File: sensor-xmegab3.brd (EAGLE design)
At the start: 55.6 x 39.3 mm, 46 parts, among them K1 SP6029TOP, M1 NRF24L01P-M, M2 DHT22-NP, Q1 IRLML2502, Q2 IRLML2502, U1 MCP1640C, X1 serial, X2 SPI/1W, X3 I2C, X4 ADC, X6 PDI

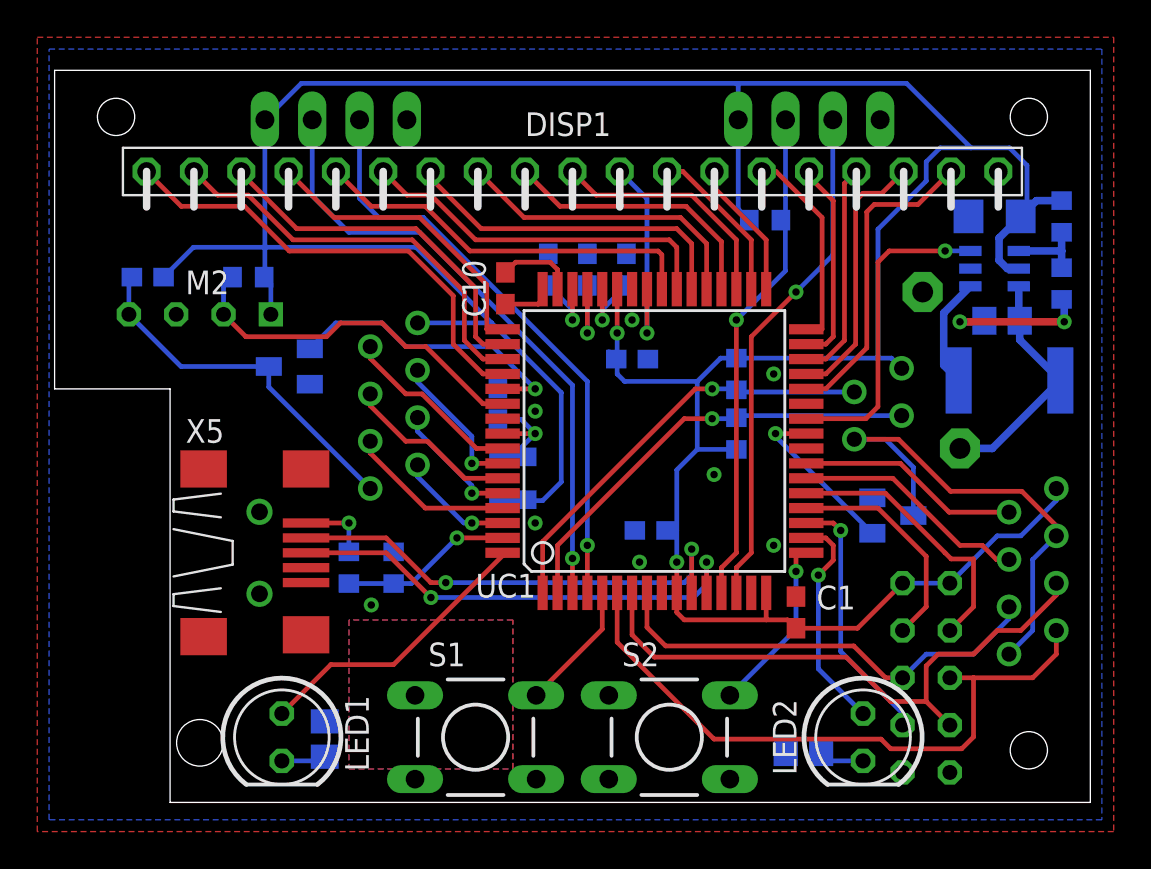
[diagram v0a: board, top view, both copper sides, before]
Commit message: pulldown for boostup enable line
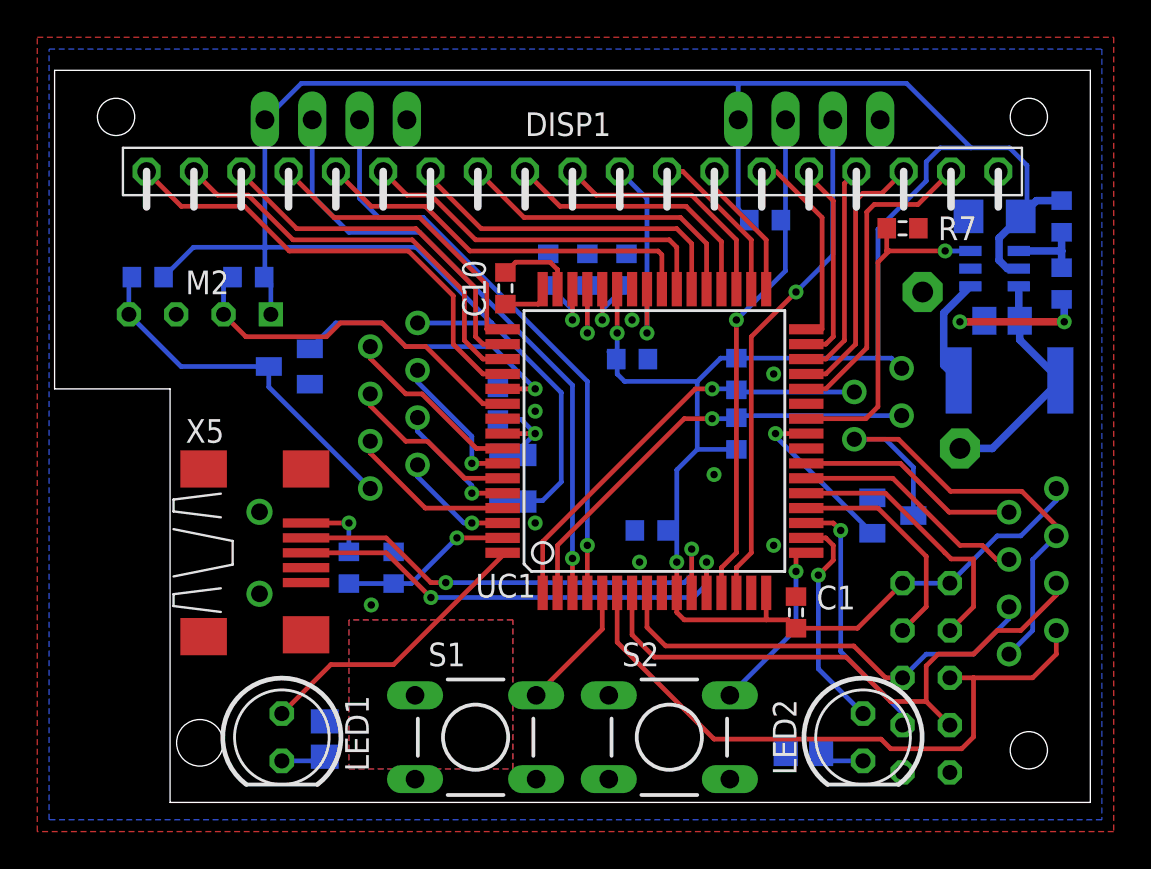
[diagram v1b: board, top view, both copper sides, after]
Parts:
- added R7: 10k, rcl:R0603
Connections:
- net GND: now also R7.2
- net PWRON: now also R7.1
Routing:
- net PWRON: track 17.1 -> 18.4 mm

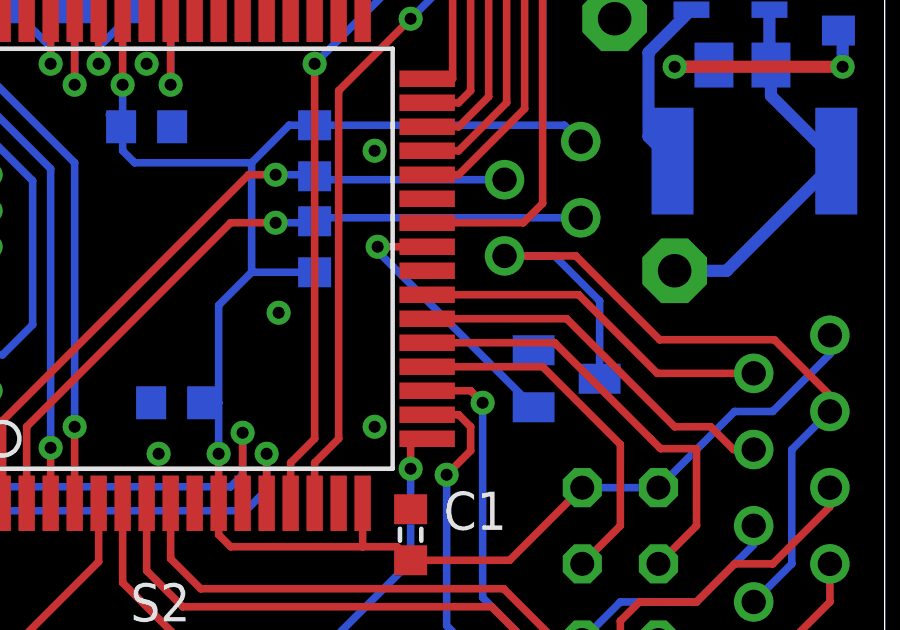
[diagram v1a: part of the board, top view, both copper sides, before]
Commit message: free seg14/15, can't be used with lcd in use
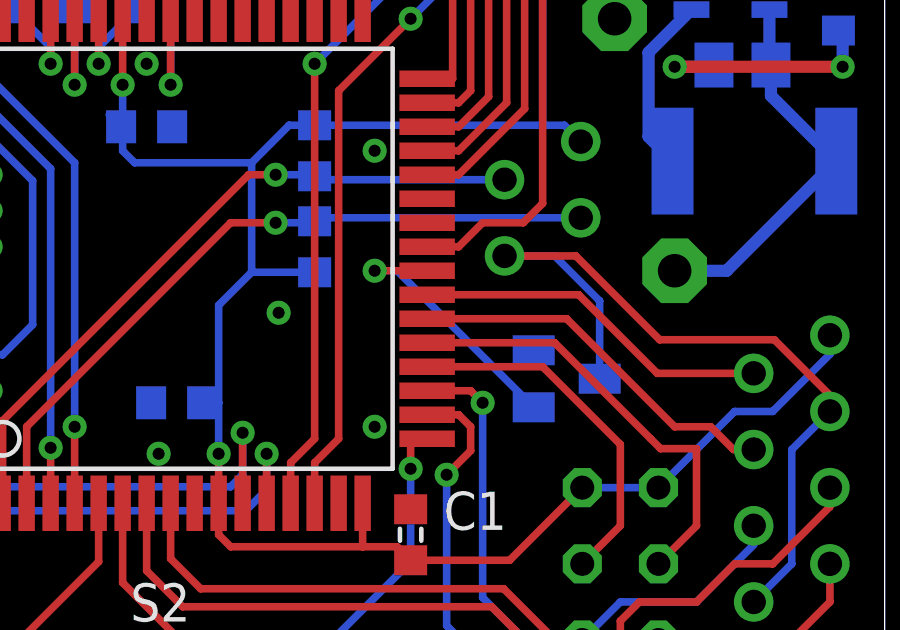
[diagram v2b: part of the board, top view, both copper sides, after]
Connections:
- new net SEG14: UC1.27
- new net SEG15: UC1.26
- net PWRON: now also UC1.25; no longer UC1.26
- net SPI1WON: now also UC1.24; no longer UC1.25
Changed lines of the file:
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@@
 <setting verticaltext="up"/>
 </settings>
-<grid distance="0.635" unitdist="mm" unit="mm" style="lines" multiple="1" display="yes" altdistance="5" altunitdist="mil" altunit="mic"/>
+<grid distance="0.4" unitdist="mm" unit="mm" style="lines" multiple="1" display="yes" altdistance="0.1" altunitdist="mm" altunit="mm"/>
 <layers>
 <layer number="1" name="Top" color="4" fill="1" visible="yes" active="yes"/>
@@
 <layer number="14" name="Route14" color="1" fill="6" visible="no" active="no"/>
 <layer number="15" name="Route15" color="4" fill="6" visible="no" active="no"/>
-<layer number="16" name="Bottom" color="1" fill="1" visible="no" active="yes"/>
+<layer number="16" name="Bottom" color="1" fill="1" visible="yes" active="yes"/>
 <layer number="17" name="Pads" color="2" fill="1" visible="yes" active="yes"/>
 <layer number="18" name="Vias" color="2" fill="1" visible="yes" active="yes"/>
@@
 <via x="48.005" y="31.805" extent="1-16" drill="0.4"/>
 <wire x1="45.005" y1="31.805" x2="48.005" y2="31.805" width="0.254" layer="1"/>
-<contactref element="UC1" pad="26"/>
-<wire x1="43.755" y1="22.8" x2="40.55" y2="22.8" width="0.254" layer="1"/>
 <contactref element="R7" pad="1"/>
 <wire x1="45.005" y1="31.805" x2="44.87" y2="31.805" width="0.254" layer="1"/>
 <wire x1="44.87" y1="31.805" x2="44.87" y2="33.02" width="0.254" layer="1"/>
+<contactref element="UC1" pad="25"/>
+<wire x1="43.755" y1="22.8" x2="42.4" y2="22.8" width="0.254" layer="1"/>
+<wire x1="42.4" y1="22.8" x2="41.6" y2="22" width="0.254" layer="1"/>
+<wire x1="41.6" y1="22" x2="40.55" y2="22" width="0.254" layer="1"/>
 </signal>
 <signal name="RFIRQ">
@@
 <contactref element="Q2" pad="1"/>
 <wire x1="44.1" y1="16.65" x2="43.75" y2="16.65" width="0.254" layer="16"/>
-<via x="38.9" y="22" extent="1-16" drill="0.4"/>
-<contactref element="UC1" pad="25"/>
-<wire x1="38.9" y1="22" x2="38.9" y2="21.85" width="0.254" layer="16"/>
-<wire x1="38.9" y1="21.85" x2="44.1" y2="16.65" width="0.254" layer="16"/>
-<wire x1="40.55" y1="22" x2="38.9" y2="22" width="0.254" layer="1"/>
+<contactref element="UC1" pad="24"/>
+<wire x1="44.1" y1="16.65" x2="39.55" y2="21.2" width="0.254" layer="16"/>
+<wire x1="39.55" y1="21.2" x2="38.8" y2="21.2" width="0.254" layer="16"/>
+<via x="38.8" y="21.2" extent="1-16" drill="0.4"/>
+<wire x1="38.8" y1="21.2" x2="40.55" y2="21.2" width="0.254" layer="1"/>
 </signal>
 <signal name="N$1">
@@
 </polygon>
 </signal>
+<signal name="SEG14">
+<contactref element="UC1" pad="27"/>
+</signal>
+<signal name="SEG15">
+<contactref element="UC1" pad="26"/>
+</signal>
 </signals>

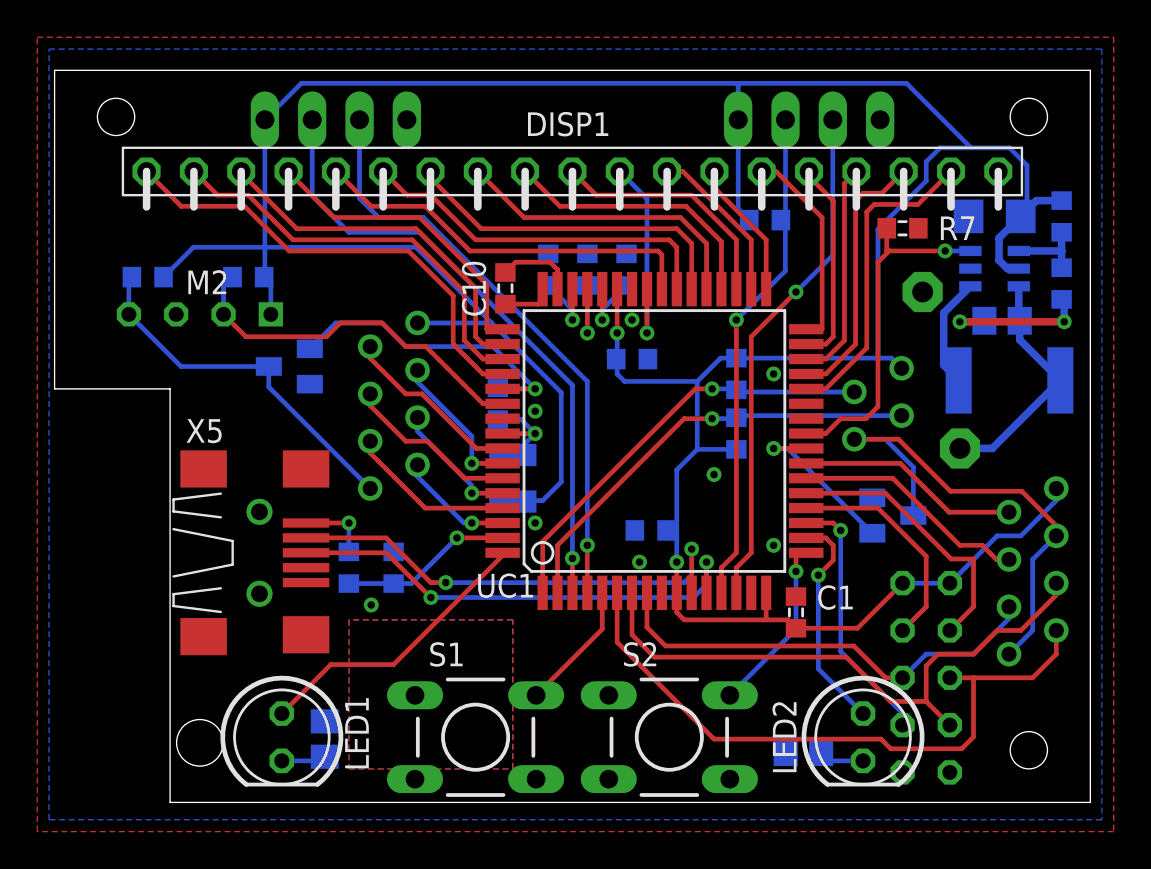
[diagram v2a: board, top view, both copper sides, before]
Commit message: reassign display pins
    fixes #1
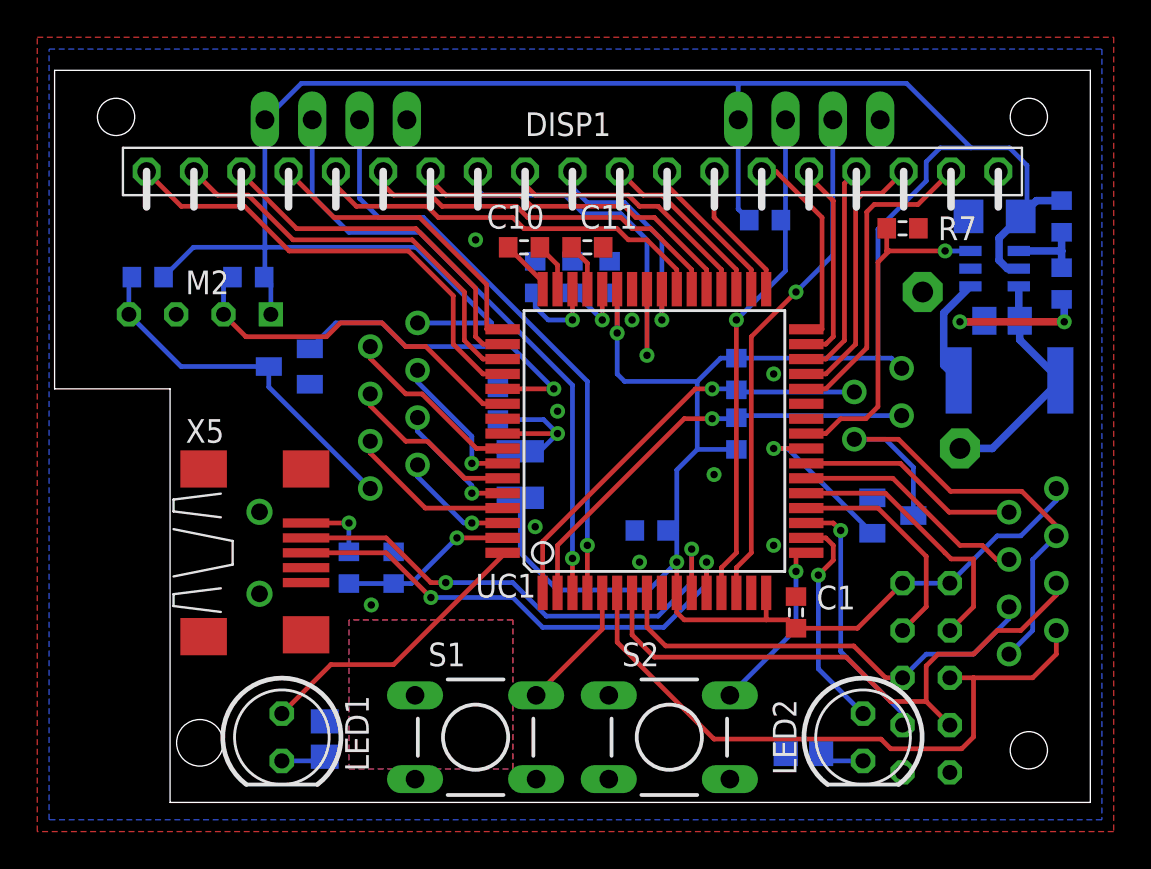
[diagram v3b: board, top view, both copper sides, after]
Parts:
- X5: value (none) -> USB
- moved C2 4.56 mm to (30.0, 30.4), turned to 90 degrees
- moved C12 2.93 mm to (28.0, 30.4)
- moved C10 2.42 mm to (25.4, 32.0), turned to 180 degrees
- moved C11 1.20 mm to (28.8, 32.0), flipped to the top, turned to 180 degrees
- moved C9 0.81 mm to (26.0, 30.4)
- moved L2 0.45 mm to (25.2, 19.8)
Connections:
- net SEG0: now also DISP1.8, UC1.41; no longer DISP1.5, UC1.40
- net SEG1: now also DISP1.10, UC1.40; no longer DISP1.6, UC1.39
- net SEG2: now also DISP1.5, UC1.39; no longer DISP1.7, UC1.38
- net SEG3: now also DISP1.6, UC1.38; no longer DISP1.8, UC1.37
- net SEG4: now also DISP1.7, UC1.37; no longer DISP1.9, UC1.36
- net SEG5: now also DISP1.9, UC1.36; no longer DISP1.10, UC1.35
- net SEG6: now also UC1.35; no longer UC1.41
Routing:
- net SEG1: track 19.7 -> 12.8 mm, vias 0 -> 1
- net SEG3: track 16.3 -> 20.2 mm
- net SEG2: track 18.3 -> 22.0 mm
- net SEG4: track 14.7 -> 18.3 mm
- net AVCC: track 5.81 -> 8.85 mm
- net N$9: track 4.90 -> 2.60 mm, vias 1 -> 0
- net DHTADCON: track 15.9 -> 17.9 mm
- net USBD_N: track 25.6 -> 27.3 mm
- net N$23: track 4.24 -> 2.64 mm
- net SEG6: track 11.6 -> 10.0 mm, vias 1 -> 0
- net VCC: track 185.8 -> 187.2 mm
- net USBD_P: track 25.6 -> 27.0 mm
- net SEG5: track 13.0 -> 14.2 mm
- net N$25: track 2.65 -> 3.57 mm
- net N$14: track 4.04 -> 4.69 mm
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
